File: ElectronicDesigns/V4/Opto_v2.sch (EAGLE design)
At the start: 5 parts, among them U1 TLV1117-18IDCYG3

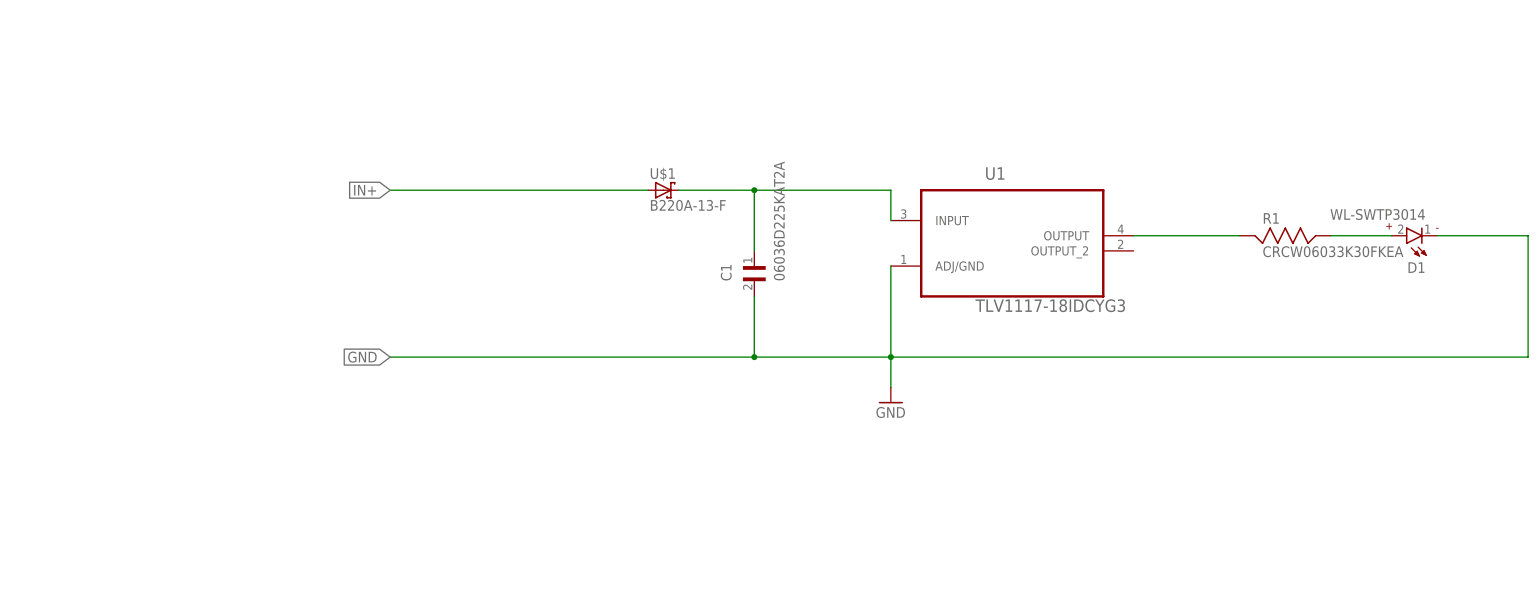
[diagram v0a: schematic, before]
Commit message: Circuit modified for antenna of Sparkfun
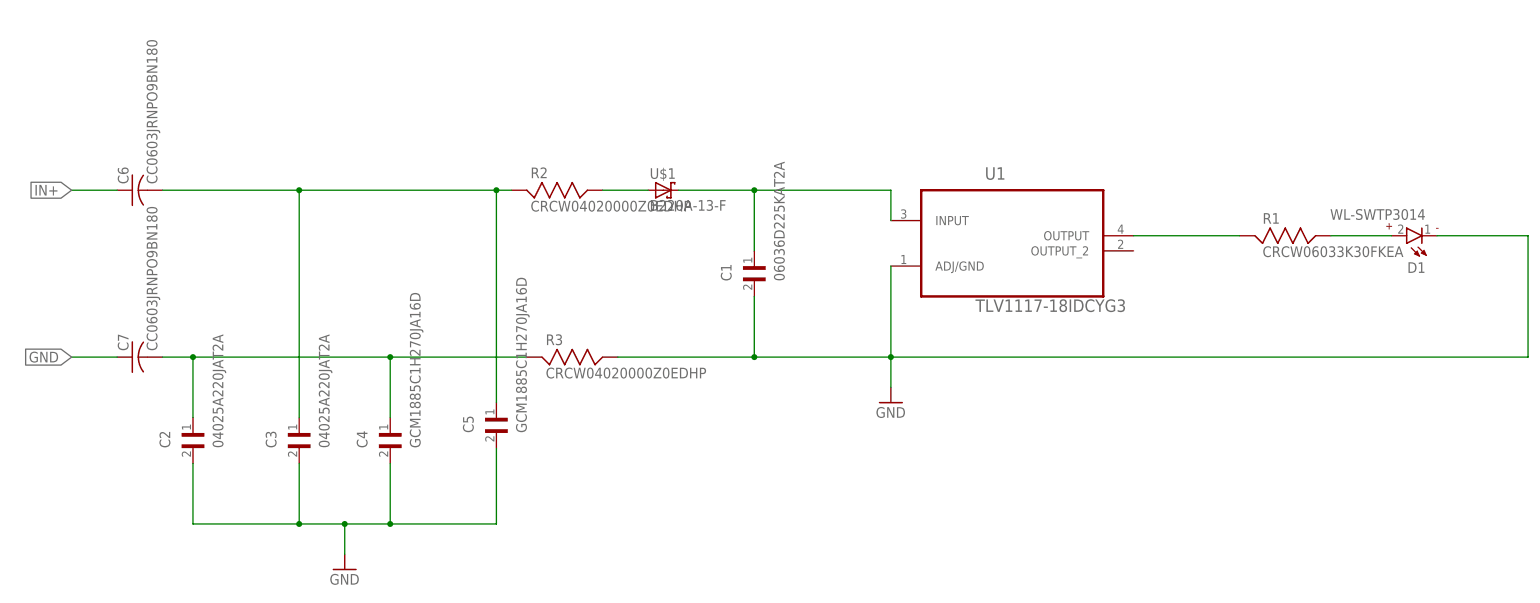
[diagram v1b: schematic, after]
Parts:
- added C2, C3: 04025A220JAT2A, 04025A220JAT2A:04025A220JAT2A
- added C4, C5: GCM1885C1H270JA16D, GCM1885C1H270JA16D:GCM1885C1H270JA16D
- added C6, C7: CC0603JRNPO9BN180, CC0603JRNPO9BN180:CC0603JRNPO9BN180
- added R2, R3: CRCW04020000Z0EDHP, CRCW04020000Z0EDHP:CRCW04020000Z0EDHP
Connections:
- new net N$3: C2.1, C4.1, C7.2, R3.1
- new net N$5: C3.1, C5.1, C6.2, R2.1
- new net N$6: R2.2, U$1.A
- net GND: now also C2.2, C3.2, C4.2, C5.2, C7.1, R3.2
- net IN+: now also C6.1; no longer U$1.A
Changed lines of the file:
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@@
 <part name="C1" library="Capacitor_2.2uF_0603" deviceset="06036D225KAT2A" device=""/>
 <part name="D1" library="WL-SWTP" deviceset="WL-SWTP" device="3014"/>
+<part name="C4" library="GCM1885C1H270JA16D" deviceset="GCM1885C1H270JA16D" device=""/>
+<part name="C5" library="GCM1885C1H270JA16D" deviceset="GCM1885C1H270JA16D" device=""/>
+<part name="C6" library="CC0603JRNPO9BN180" deviceset="CC0603JRNPO9BN180" device=""/>
+<part name="C7" library="CC0603JRNPO9BN180" deviceset="CC0603JRNPO9BN180" device=""/>
+<part name="R3" library="CRCW04020000Z0EDHP" deviceset="CRCW04020000Z0EDHP" device=""/>
+<part name="C2" library="04025A220JAT2A" deviceset="04025A220JAT2A" device=""/>
+<part name="C3" library="04025A220JAT2A" deviceset="04025A220JAT2A" device=""/>
+<part name="GND2" library="supply1" library_urn="urn:adsk.eagle:library:371" deviceset="GND" device=""/>
+<part name="R2" library="CRCW04020000Z0EDHP" deviceset="CRCW04020000Z0EDHP" device=""/>
 </parts>
 <sheets>
@@
 <instance part="C1" gate="G$1" x="25.4" y="55.88" rot="R90"/>
 <instance part="D1" gate="G$1" x="137.16" y="63.5" rot="R180"/>
+<instance part="C4" gate="G$1" x="-35.56" y="27.94" rot="R90"/>
+<instance part="C5" gate="G$1" x="-17.78" y="30.48" rot="R90"/>
+<instance part="C6" gate="G$1" x="-78.74" y="71.12" rot="R90"/>
+<instance part="C7" gate="G$1" x="-78.74" y="43.18" rot="R90"/>
+<instance part="R3" gate="G$1" x="-5.08" y="43.18"/>
+<instance part="C2" gate="G$1" x="-68.58" y="27.94" rot="R90"/>
+<instance part="C3" gate="G$1" x="-50.8" y="27.94" rot="R90"/>
+<instance part="GND2" gate="1" x="-43.18" y="7.62"/>
+<instance part="R2" gate="G$1" x="-7.62" y="71.12"/>
 </instances>
 <busses>
 </busses>
 <nets>
-<net name="IN+" class="0">
-<segment>
-<label x="-35.56" y="71.12" size="1.778" layer="95" rot="R180" xref="yes"/>
-<pinref part="U$1" gate="A" pin="A"/>
-<wire x1="7.62" y1="71.12" x2="-35.56" y2="71.12" width="0.1524" layer="91"/>
-</segment>
-</net>
 <net name="N$4" class="0">
 <segment>
@@
 <wire x1="48.26" y1="58.42" x2="48.26" y2="43.18" width="0.1524" layer="91"/>
 <wire x1="48.26" y1="43.18" x2="25.4" y2="43.18" width="0.1524" layer="91"/>
-<label x="-35.56" y="43.18" size="1.778" layer="95" rot="R180" xref="yes"/>
-<wire x1="25.4" y1="43.18" x2="-35.56" y2="43.18" width="0.1524" layer="91"/>
 <wire x1="154.94" y1="63.5" x2="154.94" y2="43.18" width="0.1524" layer="91"/>
 <wire x1="154.94" y1="43.18" x2="48.26" y2="43.18" width="0.1524" layer="91"/>
@@
 <pinref part="C1" gate="G$1" pin="2"/>
 <wire x1="25.4" y1="53.34" x2="25.4" y2="43.18" width="0.1524" layer="91"/>
-<junction x="25.4" y="43.18"/>
 <pinref part="D1" gate="G$1" pin="1"/>
 <wire x1="139.7" y1="63.5" x2="154.94" y2="63.5" width="0.1524" layer="91"/>
+<pinref part="R3" gate="G$1" pin="2"/>
+<wire x1="2.54" y1="43.18" x2="25.4" y2="43.18" width="0.1524" layer="91"/>
+<junction x="25.4" y="43.18"/>
+</segment>
+<segment>
+<pinref part="C2" gate="G$1" pin="2"/>
+<wire x1="-68.58" y1="25.4" x2="-68.58" y2="15.24" width="0.1524" layer="91"/>
+<wire x1="-68.58" y1="15.24" x2="-50.8" y2="15.24" width="0.1524" layer="91"/>
+<pinref part="C3" gate="G$1" pin="2"/>
+<wire x1="-50.8" y1="15.24" x2="-50.8" y2="25.4" width="0.1524" layer="91"/>
+<pinref part="C4" gate="G$1" pin="2"/>
+<wire x1="-50.8" y1="15.24" x2="-43.18" y2="15.24" width="0.1524" layer="91"/>
+<wire x1="-43.18" y1="15.24" x2="-35.56" y2="15.24" width="0.1524" layer="91"/>
+<wire x1="-35.56" y1="15.24" x2="-35.56" y2="25.4" width="0.1524" layer="91"/>
+<junction x="-50.8" y="15.24"/>
+<pinref part="C5" gate="G$1" pin="2"/>
+<wire x1="-17.78" y1="27.94" x2="-17.78" y2="15.24" width="0.1524" layer="91"/>
+<wire x1="-17.78" y1="15.24" x2="-35.56" y2="15.24" width="0.1524" layer="91"/>
+<junction x="-35.56" y="15.24"/>
+<pinref part="GND2" gate="1" pin="GND"/>
+<wire x1="-43.18" y1="10.16" x2="-43.18" y2="15.24" width="0.1524" layer="91"/>
+<junction x="-43.18" y="15.24"/>
+</segment>
+<segment>
+<pinref part="C7" gate="G$1" pin="1"/>
+<wire x1="-81.28" y1="43.18" x2="-88.9" y2="43.18" width="0.1524" layer="91"/>
+<label x="-88.9" y="43.18" size="1.778" layer="95" rot="R180" xref="yes"/>
 </segment>
 </net>
@@
 </segment>
 </net>
+<net name="N$3" class="0">
+<segment>
+<pinref part="C2" gate="G$1" pin="1"/>
+<pinref part="C7" gate="G$1" pin="2"/>
+<wire x1="-68.58" y1="33.02" x2="-68.58" y2="43.18" width="0.1524" layer="91"/>
+<wire x1="-68.58" y1="43.18" x2="-73.66" y2="43.18" width="0.1524" layer="91"/>
+<pinref part="C4" gate="G$1" pin="1"/>
+<wire x1="-35.56" y1="33.02" x2="-35.56" y2="43.18" width="0.1524" layer="91"/>
+<wire x1="-35.56" y1="43.18" x2="-68.58" y2="43.18" width="0.1524" layer="91"/>
+<junction x="-68.58" y="43.18"/>
+<wire x1="-12.7" y1="43.18" x2="-35.56" y2="43.18" width="0.1524" layer="91"/>
+<junction x="-35.56" y="43.18"/>
+<pinref part="R3" gate="G$1" pin="1"/>
+</segment>
+</net>
+<net name="N$5" class="0">
+<segment>
+<pinref part="C3" gate="G$1" pin="1"/>
+<pinref part="C6" gate="G$1" pin="2"/>
+<wire x1="-50.8" y1="33.02" x2="-50.8" y2="71.12" width="0.1524" layer="91"/>
+<wire x1="-50.8" y1="71.12" x2="-73.66" y2="71.12" width="0.1524" layer="91"/>
+<pinref part="C5" gate="G$1" pin="1"/>
+<wire x1="-17.78" y1="35.56" x2="-17.78" y2="71.12" width="0.1524" layer="91"/>
+<wire x1="-17.78" y1="71.12" x2="-50.8" y2="71.12" width="0.1524" layer="91"/>
+<junction x="-50.8" y="71.12"/>
+<pinref part="R2" gate="G$1" pin="1"/>
+<wire x1="-15.24" y1="71.12" x2="-17.78" y2="71.12" width="0.1524" layer="91"/>
+<junction x="-17.78" y="71.12"/>
+</segment>
+</net>
+<net name="IN+" class="0">
+<segment>
+<pinref part="C6" gate="G$1" pin="1"/>
+<wire x1="-81.28" y1="71.12" x2="-88.9" y2="71.12" width="0.1524" layer="91"/>
+<label x="-88.9" y="71.12" size="1.778" layer="95" rot="R180" xref="yes"/>
+</segment>
+</net>
+<net name="N$6" class="0">
+<segment>
+<pinref part="R2" gate="G$1" pin="2"/>
+<pinref part="U$1" gate="A" pin="A"/>
+<wire x1="0" y1="71.12" x2="7.62" y2="71.12" width="0.1524" layer="91"/>
+</segment>
+</net>
